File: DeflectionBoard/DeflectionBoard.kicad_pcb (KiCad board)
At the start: 2 copper layers, 106.2 x 50.1 mm, 93 parts, among them J1 Conn_01x04, J101 Conn_01x02, J201 YOKE, J301 YOKE, U101 TPS55340PWPR, U102 AP63205WU, U103 REF3325AIDCKT, U201 CSD97394Q4M, U202 CSD97394Q4M, U203 INA240A1D, U204 OPA2196xD, U205 TLV3501AID, U206 74LVC1G04, U207 74LVC1G08, U208 74LVC1G08, U301 CSD97394Q4M, U302 CSD97394Q4M, U303 INA240A1D, U304 OPA2196xD, U305 TLV3501AID, U306 74LVC1G04, U307 74LVC1G08, U308 74LVC1G08

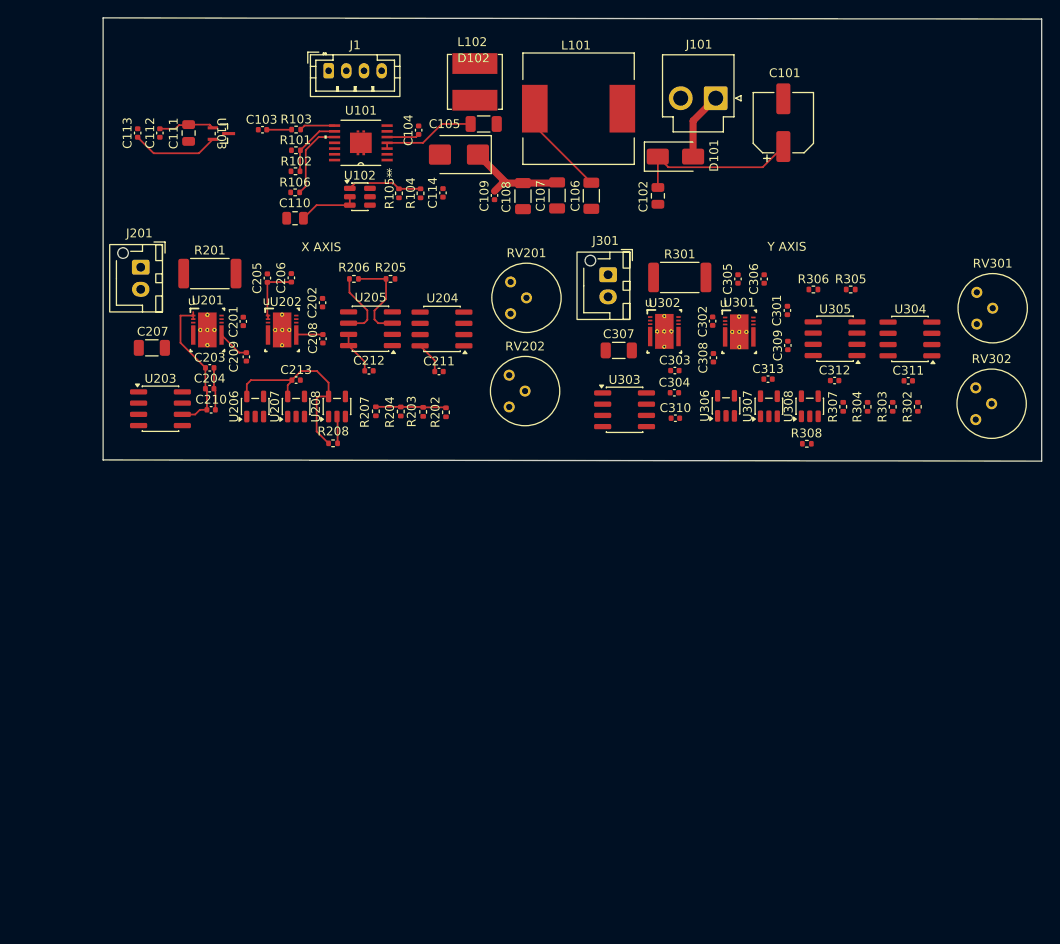
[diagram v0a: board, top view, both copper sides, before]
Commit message: DeflectionBoard: PCB placement + routing complete, DRC clean
- Anchor+satellite placement (decoupling caps hug their IC)
- Footprint fixes: DPC0008A thermal vias 0.2->0.3mm drill (JLCPCB min),
  PWP14 removed stray F.Cu polygons (EPAD short/mask-bridge)
- Project: min_resolved_spokes 2->1 (small-pad thermal relief)
- Routing complete: 0 DRC errors, 0 warnings

Co-Authored-By: Claude Opus 4.8 <noreply@anthropic.com>
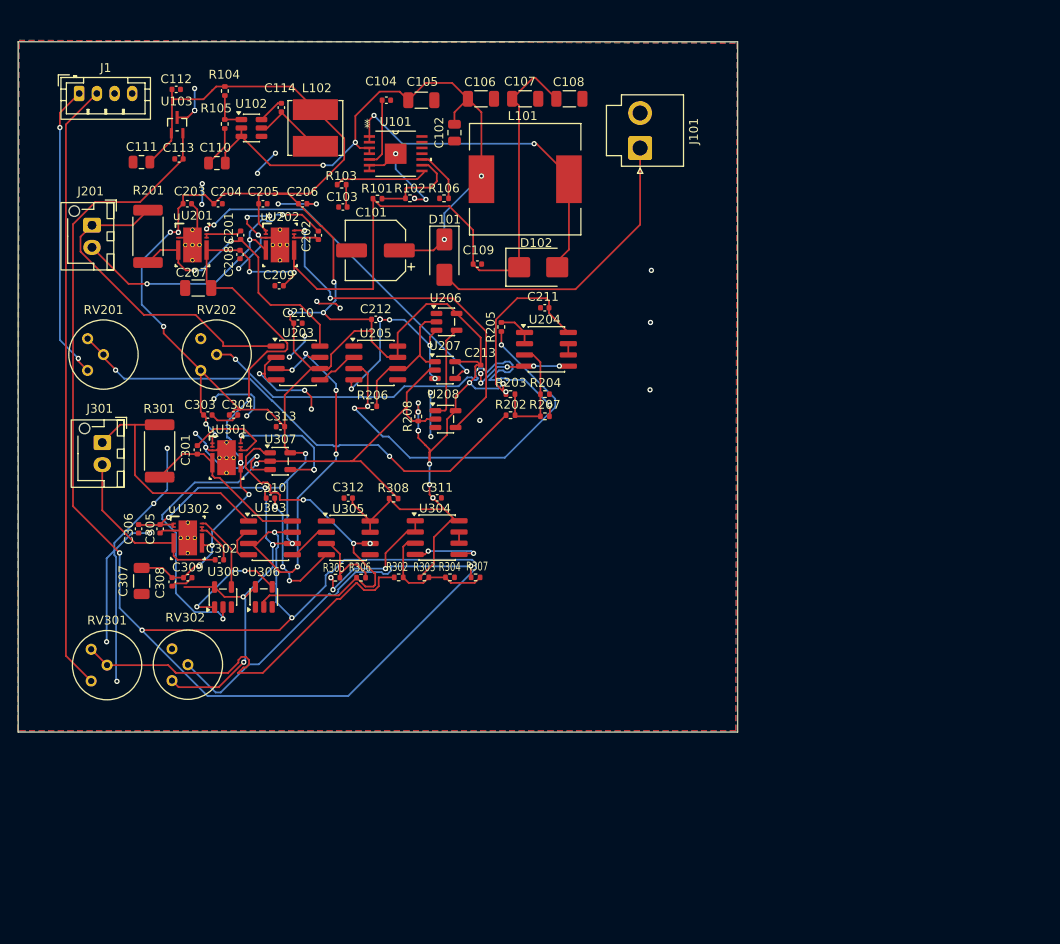
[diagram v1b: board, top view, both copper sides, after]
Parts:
- moved RV301 108.0 mm to (105.8, 109.8)
- moved RV302 95.6 mm to (115.0, 109.7)
- moved C306 76.2 mm to (111.2, 92.6), turned to -90 degrees
- moved C309 72.8 mm to (116.8, 98.1), turned to 0 degrees
- moved C305 71.2 mm to (113.6, 92.6), turned to -90 degrees
- moved U308 69.8 mm to (120.8, 100.3)
- moved C301 68.6 mm to (117.9, 83.6)
- moved R305 66.8 mm to (133.5, 98.1)
- moved C308 66.3 mm to (115.0, 98.6), turned to -90 degrees
- moved R301 62.0 mm to (113.6, 83.8), turned to 90 degrees
- moved C302 62.0 mm to (120.4, 96.1), turned to 180 degrees
- moved R302 61.8 mm to (140.6, 98.1), turned to 0 degrees
- moved R306 60.7 mm to (136.4, 98.1)
- moved J301 60.3 mm to (107.1, 82.8)
- moved C307 59.9 mm to (111.6, 98.5), turned to -90 degrees
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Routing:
- net +5V: track 61.4 -> 348.7 mm, vias 0 -> 26
- net GND: track 4.82 -> 213.4 mm, vias 0 -> 55
- net +2V5: track 9.91 -> 213.7 mm, vias 0 -> 9
- net +15V: track 19.1 -> 143.8 mm, vias 0 -> 8
- net /Deflection_Channel_Y/AXIS_IN: track 0.00 -> 69.1 mm
- net EN: track 3.06 -> 67.7 mm, vias 0 -> 2
- net Net-(R202-Pad1): track 0.00 -> 56.5 mm, vias 0 -> 2
- net Net-(R207-Pad1): track 0.00 -> 52.2 mm, vias 0 -> 2
- net Net-(R302-Pad1): track 0.00 -> 45.6 mm
- net /Deflection_Channel_Y/Q: track 0.00 -> 43.9 mm, vias 0 -> 3
- net /Deflection_Channel_X/PWM_B: track 0.00 -> 41.5 mm, vias 0 -> 2
- net Net-(R307-Pad1): track 0.00 -> 41.3 mm, vias 0 -> 1
- net /Deflection_Channel_X/PWM_A: track 0.00 -> 39.6 mm, vias 0 -> 3
- net Net-(D102-A): track 0.00 -> 38.4 mm, vias 0 -> 2
- net /Deflection_Channel_X/COIL_A: track 0.00 -> 37.3 mm
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- added copper zone on B.Cu, net GND
- added copper zone on F.Cu, net GND
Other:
- board size 106.2 x 50.1 mm -> 81.4 x 78.1 mm
- board text removed: "X AXIS"
- board text removed: "Y AXIS"

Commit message: DeflectionBoard: full PCB routing complete, DRC clean
- Channel X + Y fully routed (0 unconnected), power section + GND pour
- Power netclasses: +7.5V/+15V wide (1.8mm), +5V/yoke/SW (1.0mm), signals 0.25mm
- Manual neck-down to fine-pitch power pins; thermal/stitching vias
- Only 5 benign lib_footprint_mismatch warnings remain (no fab impact)

Co-Authored-By: Claude Opus 4.8 <noreply@anthropic.com>
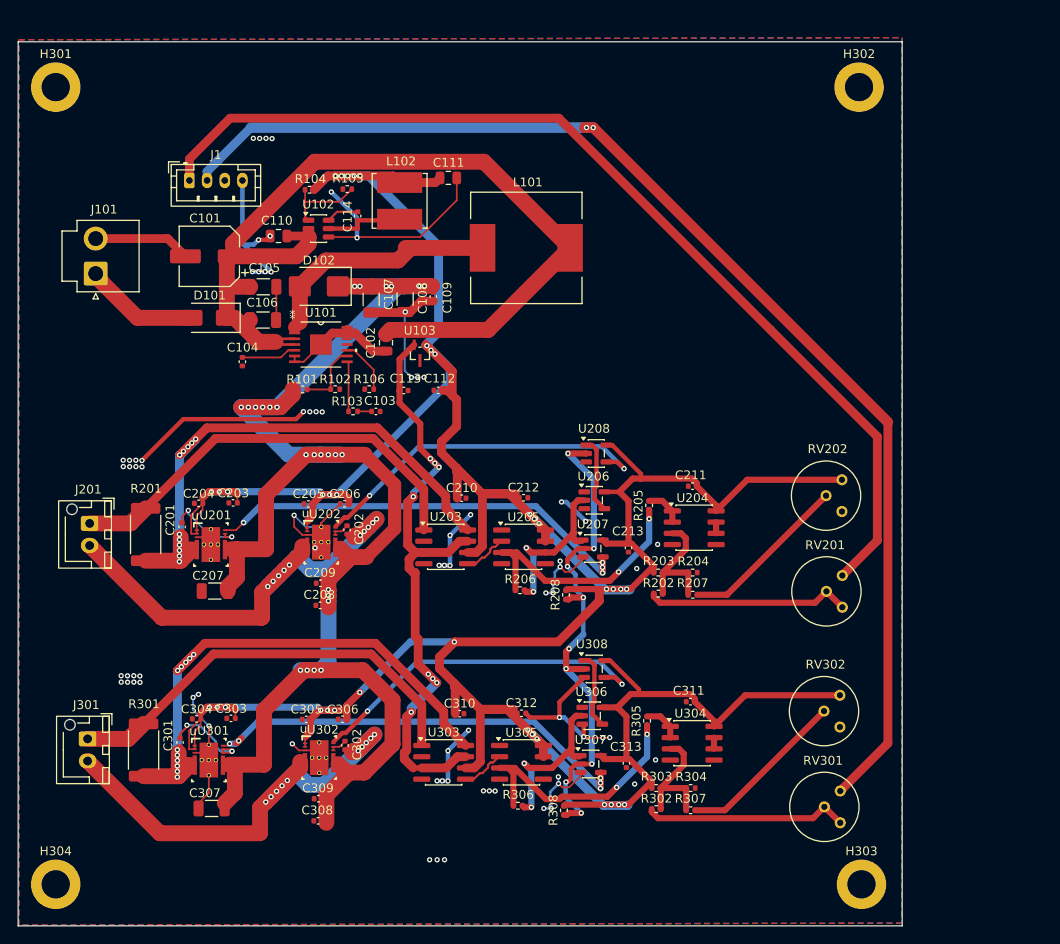
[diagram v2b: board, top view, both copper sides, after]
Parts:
- added H301: MountingHole, MountingHole:MountingHole_3.2mm_M3_DIN965_Pad, F.Cu at (101.8, 42.6)
- added H302: MountingHole, MountingHole:MountingHole_3.2mm_M3_DIN965_Pad, F.Cu at (192.7, 42.6)
- added H303: MountingHole, MountingHole:MountingHole_3.2mm_M3_DIN965_Pad, F.Cu at (193.0, 132.8)
- added H304: MountingHole, MountingHole:MountingHole_3.2mm_M3_DIN965_Pad, F.Cu at (101.8, 132.8)
- moved RV201 88.5 mm to (190.8, 97.9), turned to 180 degrees
- moved RV301 85.6 mm to (190.6, 122.2), turned to 180 degrees
- moved RV302 75.6 mm to (190.5, 111.4), turned to 180 degrees
- moved RV202 73.6 mm to (190.8, 87.0), turned to 180 degrees
- moved J101 63.2 mm to (106.4, 63.7)
- moved C313 54.6 mm to (166.4, 119.1), turned to -90 degrees
- moved U307 49.1 mm to (162.4, 119.2)
- moved C112 45.1 mm to (145.1, 76.9), turned to 180 degrees
- moved U308 42.8 mm to (162.7, 108.4), turned to 0 degrees
- moved C208 40.7 mm to (131.8, 101.2), turned to 180 degrees
- moved R308 40.2 mm to (159.3, 124.4), turned to 90 degrees
- moved U306 39.5 mm to (162.5, 113.7), turned to 0 degrees
- moved R302 39.2 mm to (169.8, 124.3)
- moved R305 38.8 mm to (168.7, 114.3), turned to -90 degrees
- moved U103 37.7 mm to (143.0, 72.7), turned to 180 degrees
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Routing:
- net +2V5: track 213.7 -> 72.4 mm, vias 9 -> 8
- net /Deflection_Channel_X/AXIS_IN: track 33.5 -> 114.4 mm, vias 2 -> 0
- net /Deflection_Channel_Y/AXIS_IN: track 69.1 -> 138.8 mm, vias 0 -> 2
- net +5V: track 348.7 -> 409.4 mm, vias 26 -> 36
- net /Deflection_Channel_Y/SW_A: track 21.7 -> 65.2 mm, vias 0 -> 11
- net +15V: track 143.8 -> 186.6 mm, vias 8 -> 25
- net +7.5V: track 68.8 -> 105.5 mm, vias 4 -> 0
- net /Deflection_Channel_Y/PWM_A: track 14.9 -> 50.7 mm, vias 3 -> 5
- net Net-(R202-Pad1): track 56.5 -> 23.2 mm, vias 2 -> 0
- net Net-(R207-Pad1): track 52.2 -> 19.2 mm, vias 2 -> 0
- net /Deflection_Channel_Y/SW_B: track 21.1 -> 52.2 mm, vias 0 -> 10
- net /Deflection_Channel_Y/PWM_B: track 8.83 -> 39.8 mm, vias 0 -> 2
- net /Deflection_Channel_X/SW_A: track 32.1 -> 62.7 mm, vias 2 -> 11
- net /Deflection_Channel_Y/Q: track 43.9 -> 19.2 mm, vias 3 -> 2
- net Net-(R302-Pad1): track 45.6 -> 23.2 mm
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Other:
- board size 81.4 x 78.1 mm -> 100 x 100 mm
